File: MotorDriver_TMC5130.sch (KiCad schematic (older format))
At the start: 17 parts, among them U8 TMC5130

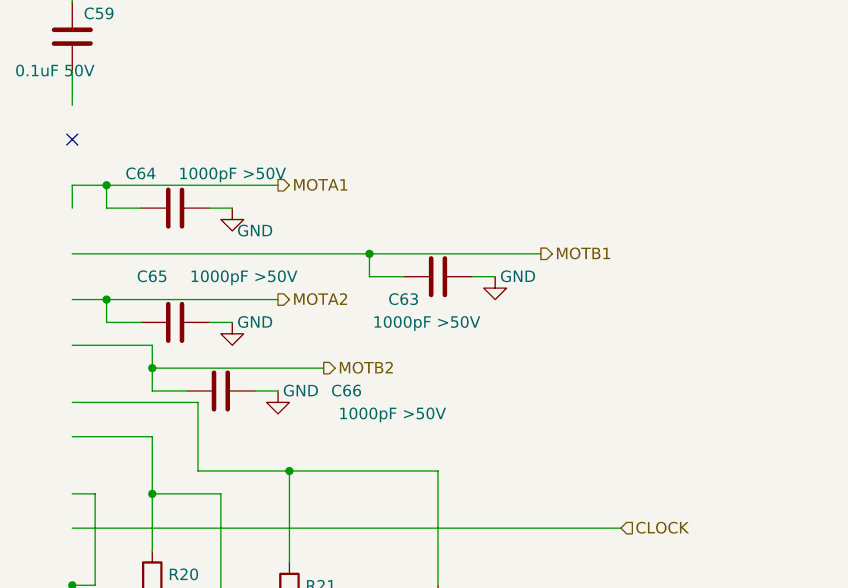
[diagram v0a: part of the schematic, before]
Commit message: Changed 1000pF capacitor value in teh motor drivers.
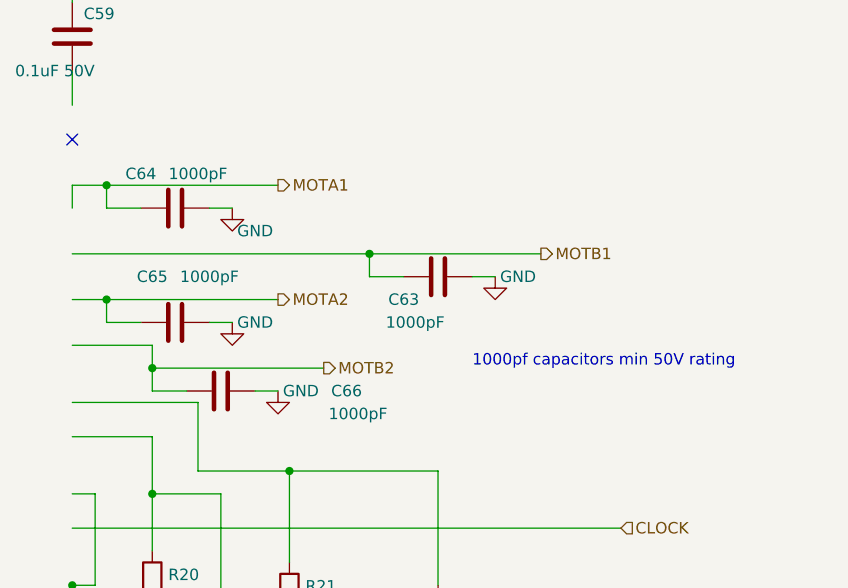
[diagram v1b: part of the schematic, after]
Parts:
- C10, C11, C12, C13: value 1000pF >50V -> 1000pF
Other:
- note added: "1000pf capacitors min 50V rating"
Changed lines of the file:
@@
 $Descr A4 11693 8268
 encoding utf-8
-Sheet 17 35
+Sheet 26 35
 Title ""
 Date ""
@@
 AR Path="/5AC337B6/5AD9F95A/5AD4B0F5/5AC33CA1" Ref="C63"  Part="1"
 F 0 "C63" V 7650 3450 50  0000 C CNN
-F 1 "1000pF >50V" V 7750 3550 50  0000 C CNN
+F 1 "1000pF" V 7750 3500 50  0000 C CNN
 F 2 "Capacitor_SMD:C_0603_1608Metric" H 7588 3450 50  0001 C CNN
 F 3 "~" H 7550 3600 50  0001 C CNN
@@
 AR Path="/5AC337B6/5AD9F95A/5AD4B0F5/5AC33D6E" Ref="C64"  Part="1"
 F 0 "C64" V 6250 3150 50  0000 C CNN
-F 1 "1000pF >50V" V 6250 3550 50  0000 C CNN
+F 1 "1000pF" V 6250 3400 50  0000 C CNN
 F 2 "Capacitor_SMD:C_0603_1608Metric" H 6438 3150 50  0001 C CNN
 F 3 "~" H 6400 3300 50  0001 C CNN
@@
 AR Path="/5AC337B6/5AD9F95A/5AD4B0F5/5AC33DC1" Ref="C65"  Part="1"
 F 0 "C65" V 6200 3700 50  0000 C CNN
-F 1 "1000pF >50V" V 6200 4100 50  0000 C CNN
+F 1 "1000pF" V 6200 3950 50  0000 C CNN
 F 2 "Capacitor_SMD:C_0603_1608Metric" H 6438 3650 50  0001 C CNN
 F 3 "~" H 6400 3800 50  0001 C CNN
@@
 AR Path="/5AC337B6/5AD9F95A/5AD4B0F5/5AC33E6E" Ref="C66"  Part="1"
 F 0 "C66" V 6600 4650 50  0000 C CNN
-F 1 "1000pF >50V" V 6700 4850 50  0000 C CNN
+F 1 "1000pF" V 6700 4700 50  0000 C CNN
 F 2 "Capacitor_SMD:C_0603_1608Metric" H 6638 3950 50  0001 C CNN
 F 3 "~" H 6600 4100 50  0001 C CNN
@@
 Wire Wire Line
 	5950 4700 8350 4700
+Text Notes 7700 4000 0    50   ~ 0
+1000pf capacitors min 50V rating
 $EndSCHEMATC

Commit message: Switch away from rounded rect pads. The PCB boar house had issues making the board.
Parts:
- C10, C11, C12, C13, C7, C8, C84, C85: footprint Capacitor_SMD:C_0603_1608Metric -> PrntrBoardV1:C_0603_1608Metric
- C4, C74: footprint Capacitor_SMD:C_1206_3216Metric -> PrntrBoardV1:C_1206_3216Metric
- C6, C86, C87: footprint Capacitor_SMD:C_0402_1005Metric -> PrntrBoardV1:C_0402_1005Metric
- R20, R21: footprint Resistor_SMD:R_1206_3216Metric -> PrntrBoardV1:R_1206_3216Metric
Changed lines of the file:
@@
 AR Path="/5AC337B6/5ACE1C6D/5ACC0B66/5AC33A94" Ref="C46"  Part="1"
 AR Path="/5AC337B6/5AD9F95A/5AD4B0F5/5AC33A94" Ref="C59"  Part="1"
-F 0 "C59" H 6000 2650 50  0000 L CNN
+F 0 "C6" H 6000 2650 50  0000 L CNN
 F 1 "0.1uF 50V" H 5700 2400 50  0000 L CNN
-F 2 "Capacitor_SMD:C_0402_1005Metric" H 5988 2400 50  0001 C CNN
+F 2 "PrntrBoardV1:C_0402_1005Metric" H 5988 2400 50  0001 C CNN
 F 3 "~" H 5950 2550 50  0001 C CNN
 	1    5950 2550
@@
 AR Path="/5AC337B6/5ACE1C6D/5ACC0B66/5AC33B3C" Ref="C44"  Part="1"
 AR Path="/5AC337B6/5AD9F95A/5AD4B0F5/5AC33B3C" Ref="C57"  Part="1"
-F 0 "C57" H 3050 1750 50  0000 L CNN
+F 0 "C4" H 3050 1750 50  0000 L CNN
 F 1 "10uF 50V" H 2850 1650 50  0000 L CNN
-F 2 "Capacitor_SMD:C_1206_3216Metric" H 3338 1550 50  0001 C CNN
+F 2 "PrntrBoardV1:C_1206_3216Metric" H 3338 1550 50  0001 C CNN
 F 3 "~" H 3300 1700 50  0001 C CNN
 	1    3300 1700
@@
 AR Path="/5AC337B6/5ACE1C6D/5ACC0B66/5AC33B85" Ref="C47"  Part="1"
 AR Path="/5AC337B6/5AD9F95A/5AD4B0F5/5AC33B85" Ref="C60"  Part="1"
-F 0 "C60" H 5250 1800 50  0000 C CNN
+F 0 "C7" H 5250 1800 50  0000 C CNN
 F 1 "0.47uF" H 5200 1700 50  0000 C CNN
-F 2 "Capacitor_SMD:C_0603_1608Metric" H 5488 1650 50  0001 C CNN
+F 2 "PrntrBoardV1:C_0603_1608Metric" H 5488 1650 50  0001 C CNN
 F 3 "~" H 5450 1800 50  0001 C CNN
 	1    5450 1800
@@
 AR Path="/5AC337B6/5ACE1C6D/5ACC0B66/5AC33C56" Ref="C48"  Part="1"
 AR Path="/5AC337B6/5AD9F95A/5AD4B0F5/5AC33C56" Ref="C61"  Part="1"
-F 0 "C61" H 4315 2096 50  0000 L CNN
+F 0 "C8" H 4315 2096 50  0000 L CNN
 F 1 "0.1uF" H 4315 2005 50  0000 L CNN
-F 2 "Capacitor_SMD:C_0603_1608Metric" H 4238 1900 50  0001 C CNN
+F 2 "PrntrBoardV1:C_0603_1608Metric" H 4238 1900 50  0001 C CNN
 F 3 "~" H 4200 2050 50  0001 C CNN
 	1    4200 2050
@@
 AR Path="/5AC337B6/5ACE1C6D/5ACC0B66/5AC33CA1" Ref="C50"  Part="1"
 AR Path="/5AC337B6/5AD9F95A/5AD4B0F5/5AC33CA1" Ref="C63"  Part="1"
-F 0 "C63" V 7650 3450 50  0000 C CNN
+F 0 "C10" V 7650 3450 50  0000 C CNN
 F 1 "1000pF" V 7750 3500 50  0000 C CNN
-F 2 "Capacitor_SMD:C_0603_1608Metric" H 7588 3450 50  0001 C CNN
+F 2 "PrntrBoardV1:C_0603_1608Metric" H 7588 3450 50  0001 C CNN
 F 3 "~" H 7550 3600 50  0001 C CNN
 	1    7550 3600
@@
 AR Path="/5AC337B6/5ACE1C6D/5ACC0B66/5AC33D6E" Ref="C51"  Part="1"
 AR Path="/5AC337B6/5AD9F95A/5AD4B0F5/5AC33D6E" Ref="C64"  Part="1"
-F 0 "C64" V 6250 3150 50  0000 C CNN
+F 0 "C11" V 6250 3150 50  0000 C CNN
 F 1 "1000pF" V 6250 3400 50  0000 C CNN
-F 2 "Capacitor_SMD:C_0603_1608Metric" H 6438 3150 50  0001 C CNN
+F 2 "PrntrBoardV1:C_0603_1608Metric" H 6438 3150 50  0001 C CNN
 F 3 "~" H 6400 3300 50  0001 C CNN
 	1    6400 3300
@@
 AR Path="/5AC337B6/5ACE1C6D/5ACC0B66/5AC33DC1" Ref="C52"  Part="1"
 AR Path="/5AC337B6/5AD9F95A/5AD4B0F5/5AC33DC1" Ref="C65"  Part="1"
-F 0 "C65" V 6200 3700 50  0000 C CNN
+F 0 "C12" V 6200 3700 50  0000 C CNN
 F 1 "1000pF" V 6200 3950 50  0000 C CNN
-F 2 "Capacitor_SMD:C_0603_1608Metric" H 6438 3650 50  0001 C CNN
+F 2 "PrntrBoardV1:C_0603_1608Metric" H 6438 3650 50  0001 C CNN
 F 3 "~" H 6400 3800 50  0001 C CNN
 	1    6400 3800
@@
 AR Path="/5AC337B6/5ACE1C6D/5ACC0B66/5AC33E6E" Ref="C53"  Part="1"
 AR Path="/5AC337B6/5AD9F95A/5AD4B0F5/5AC33E6E" Ref="C66"  Part="1"
-F 0 "C66" V 6600 4650 50  0000 C CNN
+F 0 "C13" V 6600 4650 50  0000 C CNN
 F 1 "1000pF" V 6700 4700 50  0000 C CNN
-F 2 "Capacitor_SMD:C_0603_1608Metric" H 6638 3950 50  0001 C CNN
+F 2 "PrntrBoardV1:C_0603_1608Metric" H 6638 3950 50  0001 C CNN
 F 3 "~" H 6600 4100 50  0001 C CNN
 	1    6600 4100
@@
 AR Path="/5AC337B6/5ACE1C6D/5ACC0B66/5AC34593" Ref="#PWR049"  Part="1"
 AR Path="/5AC337B6/5AD9F95A/5AD4B0F5/5AC34593" Ref="#PWR059"  Part="1"
-F 0 "#PWR059" H 5450 1950 50  0001 C CNN
+F 0 "#PWR014" H 5450 1950 50  0001 C CNN
 F 1 "GND" H 5455 2027 50  0000 C CNN
 F 2 "" H 5450 2200 50  0001 C CNN
@@
 AR Path="/5AC337B6/5ACE1C6D/5ACC0B66/5AC345D6" Ref="#PWR048"  Part="1"
 AR Path="/5AC337B6/5AD9F95A/5AD4B0F5/5AC345D6" Ref="#PWR058"  Part="1"
-F 0 "#PWR058" H 3300 1800 50  0001 C CNN
+F 0 "#PWR013" H 3300 1800 50  0001 C CNN
 F 1 "GND" H 3305 1877 50  0000 C CNN
 F 2 "" H 3300 2050 50  0001 C CNN
@@
 AR Path="/5AC337B6/5ACE1C6D/5ACC0B66/5AC34619" Ref="#PWR050"  Part="1"
 AR Path="/5AC337B6/5AD9F95A/5AD4B0F5/5AC34619" Ref="#PWR060"  Part="1"
-F 0 "#PWR060" H 7800 3350 50  0001 C CNN
+F 0 "#PWR015" H 7800 3350 50  0001 C CNN
 F 1 "GND" H 7900 3600 50  0000 C CNN
 F 2 "" H 7800 3600 50  0001 C CNN
@@
 AR Path="/5AC337B6/5ACE1C6D/5ACC0B66/5AC3465C" Ref="#PWR051"  Part="1"
 AR Path="/5AC337B6/5AD9F95A/5AD4B0F5/5AC3465C" Ref="#PWR061"  Part="1"
-F 0 "#PWR061" H 6650 3050 50  0001 C CNN
+F 0 "#PWR016" H 6650 3050 50  0001 C CNN
 F 1 "GND" H 6750 3200 50  0000 C CNN
 F 2 "" H 6650 3300 50  0001 C CNN
@@
 AR Path="/5AC337B6/5ACE1C6D/5ACC0B66/5AC3469F" Ref="#PWR052"  Part="1"
 AR Path="/5AC337B6/5AD9F95A/5AD4B0F5/5AC3469F" Ref="#PWR062"  Part="1"
-F 0 "#PWR062" H 6650 3550 50  0001 C CNN
+F 0 "#PWR017" H 6650 3550 50  0001 C CNN
 F 1 "GND" H 6750 3800 50  0000 C CNN
 F 2 "" H 6650 3800 50  0001 C CNN
@@
 AR Path="/5AC337B6/5ACE1C6D/5ACC0B66/5AC346E2" Ref="#PWR053"  Part="1"
 AR Path="/5AC337B6/5AD9F95A/5AD4B0F5/5AC346E2" Ref="#PWR063"  Part="1"
-F 0 "#PWR063" H 6850 3850 50  0001 C CNN
+F 0 "#PWR018" H 6850 3850 50  0001 C CNN
 F 1 "GND" H 6950 4100 50  0000 C CNN
 F 2 "" H 6850 4100 50  0001 C CNN
@@
 AR Path="/5AC337B6/5ACE1C6D/5ACC0B66/5AC34725" Ref="#PWR047"  Part="1"
 AR Path="/5AC337B6/5AD9F95A/5AD4B0F5/5AC34725" Ref="#PWR057"  Part="1"
-F 0 "#PWR057" H 5350 5550 50  0001 C CNN
+F 0 "#PWR012" H 5350 5550 50  0001 C CNN
 F 1 "GND" H 5355 5627 50  0000 C CNN
 F 2 "" H 5350 5800 50  0001 C CNN
@@
 AR Path="/5AC337B6/5ACE1C6D/5ACC0B66/5AC55FA7" Ref="C45"  Part="1"
 AR Path="/5AC337B6/5AD9F95A/5AD4B0F5/5AC55FA7" Ref="C58"  Part="1"
-F 0 "C58" H 3700 1900 50  0000 L CNN
+F 0 "C5" H 3700 1900 50  0000 L CNN
 F 1 "100uF 35V" H 3700 1800 50  0000 L CNN
 F 2 "Capacitor_SMD:CP_Elec_6.3x7.7" H 3650 1700 50  0001 C CNN
@@
 AR Path="/5AC337B6/5ACE1C6D/5ACC0B66/5ACA36B2" Ref="C76"  Part="1"
 AR Path="/5AC337B6/5AD9F95A/5AD4B0F5/5ACA36B2" Ref="C77"  Part="1"
-F 0 "C77" H 2715 1746 50  0000 L CNN
+F 0 "C73" H 2715 1746 50  0000 L CNN
 F 1 "10uF 50V" H 2650 1550 50  0000 L CNN
-F 2 "Capacitor_SMD:C_1206_3216Metric" H 2638 1550 50  0001 C CNN
+F 2 "PrntrBoardV1:C_1206_3216Metric" H 2638 1550 50  0001 C CNN
 F 3 "~" H 2600 1700 50  0001 C CNN
 	1    2600 1700
@@
 AR Path="/5AC337B6/5ACCA309/5ACC0B66/5ACFA54E" Ref="U6"  Part="1"
 AR Path="/5AC337B6/5ACE1C6D/5ACC0B66/5ACFA54E" Ref="U7"  Part="1"
-F 0 "U8" H 4900 1714 50  0000 C CNN
+F 0 "U4" H 4900 1714 50  0000 C CNN
 F 1 "TMC5130" H 4900 1623 50  0000 C CNN
 F 2 "PrntrBoardV1:tmc5130-nc" H 4900 3700 50  0001 C CNN
@@
 AR Path="/5AC337B6/5ACCA309/5ACC0B66/5AD3397E" Ref="#PWR081"  Part="1"
 AR Path="/5AC337B6/5ACE1C6D/5ACC0B66/5AD3397E" Ref="#PWR083"  Part="1"
-F 0 "#PWR085" H 4200 2000 50  0001 C CNN
+F 0 "#PWR077" H 4200 2000 50  0001 C CNN
 F 1 "GND" H 4205 2077 50  0000 C CNN
 F 2 "" H 4200 2250 50  0001 C CNN
@@
 AR Path="/5AC337B6/5ACCA309/5ACC0B66/5AD37DE9" Ref="C67"  Part="1"
 AR Path="/5AC337B6/5ACE1C6D/5ACC0B66/5AD37DE9" Ref="C81"  Part="1"
-F 0 "C85" H 5000 2350 50  0000 L CNN
+F 0 "C14" H 5000 2350 50  0000 L CNN
 F 1 "0.1uF" H 4900 2250 50  0000 L CNN
-F 2 "Capacitor_SMD:C_0603_1608Metric" H 5188 2000 50  0001 C CNN
+F 2 "PrntrBoardV1:C_0603_1608Metric" H 5188 2000 50  0001 C CNN
 F 3 "~" H 5150 2150 50  0001 C CNN
 	1    5150 2150
@@
 AR Path="/5AC337B6/5ACCA309/5ACC0B66/5AD494C8" Ref="C62"  Part="1"
 AR Path="/5AC337B6/5ACE1C6D/5ACC0B66/5AD494C8" Ref="C80"  Part="1"
-F 0 "C84" V 3750 5200 50  0000 C CNN
+F 0 "C9" V 3750 5200 50  0000 C CNN
 F 1 "0.022uF 50V" V 3750 4750 50  0000 C CNN
-F 2 "Capacitor_SMD:C_0603_1608Metric" H 3638 4900 50  0001 C CNN
+F 2 "PrntrBoardV1:C_0603_1608Metric" H 3638 4900 50  0001 C CNN
 F 3 "~" H 3600 5050 50  0001 C CNN
 	1    3600 5050
@@
 AR Path="/5AC337B6/5ACCA309/5ACC0B66/5AD5670C" Ref="#PWR080"  Part="1"
 AR Path="/5AC337B6/5ACE1C6D/5ACC0B66/5AD5670C" Ref="#PWR082"  Part="1"
-F 0 "#PWR084" H 3600 3900 50  0001 C CNN
+F 0 "#PWR076" H 3600 3900 50  0001 C CNN
 F 1 "GND" H 3605 3977 50  0000 C CNN
 F 2 "" H 3600 4150 50  0001 C CNN
@@
 AR Path="/5AC337B6/5ACCA309/5ACC0B66/5AD66FAA" Ref="R12"  Part="1"
 AR Path="/5AC337B6/5ACE1C6D/5ACC0B66/5AD66FAA" Ref="R14"  Part="1"
-F 0 "R20" H 6370 4996 50  0000 L CNN
+F 0 "R2" H 6370 4996 50  0000 L CNN
 F 1 "0R15 0.5W" H 6100 4800 50  0000 L CNN
-F 2 "Resistor_SMD:R_1206_3216Metric" V 6230 4950 50  0001 C CNN
+F 2 "PrntrBoardV1:R_1206_3216Metric" V 6230 4950 50  0001 C CNN
 F 3 "~" H 6300 4950 50  0001 C CNN
 	1    6300 4950
@@
 AR Path="/5AC337B6/5ACCA309/5ACC0B66/5AD67008" Ref="R13"  Part="1"
 AR Path="/5AC337B6/5ACE1C6D/5ACC0B66/5AD67008" Ref="R15"  Part="1"
-F 0 "R21" H 6970 5046 50  0000 L CNN
+F 0 "R3" H 6970 5046 50  0000 L CNN
 F 1 "0R15 0.5W" H 6970 4955 50  0000 L CNN
-F 2 "Resistor_SMD:R_1206_3216Metric" V 6830 5000 50  0001 C CNN
+F 2 "PrntrBoardV1:R_1206_3216Metric" V 6830 5000 50  0001 C CNN
 F 3 "~" H 6900 5000 50  0001 C CNN
 	1    6900 5000
@@
 AR Path="/5AC337B6/5ACCA309/5ACC0B66/5AD6F856" Ref="C79"  Part="1"
 AR Path="/5AC337B6/5ACE1C6D/5ACC0B66/5AD6F856" Ref="C83"  Part="1"
-F 0 "C87" H 7665 5146 50  0000 L CNN
+F 0 "C28" H 7665 5146 50  0000 L CNN
 F 1 "0.1uF 50V" H 7665 5055 50  0000 L CNN
-F 2 "Capacitor_SMD:C_0402_1005Metric" H 7588 4950 50  0001 C CNN
+F 2 "PrntrBoardV1:C_0402_1005Metric" H 7588 4950 50  0001 C CNN
 F 3 "~" H 7550 5100 50  0001 C CNN
 	1    7550 5100
@@
 AR Path="/5AC337B6/5ACCA309/5ACC0B66/5AD6F966" Ref="C78"  Part="1"
 AR Path="/5AC337B6/5ACE1C6D/5ACC0B66/5AD6F966" Ref="C82"  Part="1"
-F 0 "C86" H 6715 5246 50  0000 L CNN
+F 0 "C23" H 6715 5246 50  0000 L CNN
 F 1 "0.1uF 50V" H 6350 5050 50  0000 L CNN
-F 2 "Capacitor_SMD:C_0402_1005Metric" H 6638 5050 50  0001 C CNN
+F 2 "PrntrBoardV1:C_0402_1005Metric" H 6638 5050 50  0001 C CNN
 F 3 "~" H 6600 5200 50  0001 C CNN
 	1    6600 5200

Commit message: Update schematics to match rev3 of tmc2130 branch.
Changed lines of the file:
@@
 EESchema Schematic File Version 4
 LIBS:PrntrBoardV1-cache
-EELAYER 26 0
+EELAYER 29 0
 EELAYER END
 $Descr A4 11693 8268
@@
 AR Path="/5AC337B6/5ACE1C6D/5ACC0B66/5AC33A94" Ref="C46"  Part="1"
 AR Path="/5AC337B6/5AD9F95A/5AD4B0F5/5AC33A94" Ref="C59"  Part="1"
-F 0 "C6" H 6000 2650 50  0000 L CNN
+F 0 "C59" H 6000 2650 50  0000 L CNN
 F 1 "0.1uF 50V" H 5700 2400 50  0000 L CNN
 F 2 "PrntrBoardV1:C_0402_1005Metric" H 5988 2400 50  0001 C CNN
@@
 AR Path="/5AC337B6/5ACE1C6D/5ACC0B66/5AC33B3C" Ref="C44"  Part="1"
 AR Path="/5AC337B6/5AD9F95A/5AD4B0F5/5AC33B3C" Ref="C57"  Part="1"
-F 0 "C4" H 3050 1750 50  0000 L CNN
+F 0 "C57" H 3050 1750 50  0000 L CNN
 F 1 "10uF 50V" H 2850 1650 50  0000 L CNN
 F 2 "PrntrBoardV1:C_1206_3216Metric" H 3338 1550 50  0001 C CNN
@@
 AR Path="/5AC337B6/5ACE1C6D/5ACC0B66/5AC33B85" Ref="C47"  Part="1"
 AR Path="/5AC337B6/5AD9F95A/5AD4B0F5/5AC33B85" Ref="C60"  Part="1"
-F 0 "C7" H 5250 1800 50  0000 C CNN
+F 0 "C60" H 5250 1800 50  0000 C CNN
 F 1 "0.47uF" H 5200 1700 50  0000 C CNN
 F 2 "PrntrBoardV1:C_0603_1608Metric" H 5488 1650 50  0001 C CNN
@@
 AR Path="/5AC337B6/5ACE1C6D/5ACC0B66/5AC33C56" Ref="C48"  Part="1"
 AR Path="/5AC337B6/5AD9F95A/5AD4B0F5/5AC33C56" Ref="C61"  Part="1"
-F 0 "C8" H 4315 2096 50  0000 L CNN
+F 0 "C61" H 4315 2096 50  0000 L CNN
 F 1 "0.1uF" H 4315 2005 50  0000 L CNN
 F 2 "PrntrBoardV1:C_0603_1608Metric" H 4238 1900 50  0001 C CNN
@@
 AR Path="/5AC337B6/5ACE1C6D/5ACC0B66/5AC33CA1" Ref="C50"  Part="1"
 AR Path="/5AC337B6/5AD9F95A/5AD4B0F5/5AC33CA1" Ref="C63"  Part="1"
-F 0 "C10" V 7650 3450 50  0000 C CNN
+F 0 "C63" V 7650 3450 50  0000 C CNN
 F 1 "1000pF" V 7750 3500 50  0000 C CNN
 F 2 "PrntrBoardV1:C_0603_1608Metric" H 7588 3450 50  0001 C CNN
@@
 AR Path="/5AC337B6/5ACE1C6D/5ACC0B66/5AC33D6E" Ref="C51"  Part="1"
 AR Path="/5AC337B6/5AD9F95A/5AD4B0F5/5AC33D6E" Ref="C64"  Part="1"
-F 0 "C11" V 6250 3150 50  0000 C CNN
+F 0 "C64" V 6250 3150 50  0000 C CNN
 F 1 "1000pF" V 6250 3400 50  0000 C CNN
 F 2 "PrntrBoardV1:C_0603_1608Metric" H 6438 3150 50  0001 C CNN
@@
 AR Path="/5AC337B6/5ACE1C6D/5ACC0B66/5AC33DC1" Ref="C52"  Part="1"
 AR Path="/5AC337B6/5AD9F95A/5AD4B0F5/5AC33DC1" Ref="C65"  Part="1"
-F 0 "C12" V 6200 3700 50  0000 C CNN
+F 0 "C65" V 6200 3700 50  0000 C CNN
 F 1 "1000pF" V 6200 3950 50  0000 C CNN
 F 2 "PrntrBoardV1:C_0603_1608Metric" H 6438 3650 50  0001 C CNN
@@
 AR Path="/5AC337B6/5ACE1C6D/5ACC0B66/5AC33E6E" Ref="C53"  Part="1"
 AR Path="/5AC337B6/5AD9F95A/5AD4B0F5/5AC33E6E" Ref="C66"  Part="1"
-F 0 "C13" V 6600 4650 50  0000 C CNN
+F 0 "C66" V 6600 4650 50  0000 C CNN
 F 1 "1000pF" V 6700 4700 50  0000 C CNN
 F 2 "PrntrBoardV1:C_0603_1608Metric" H 6638 3950 50  0001 C CNN
@@
 AR Path="/5AC337B6/5ACE1C6D/5ACC0B66/5AC34593" Ref="#PWR049"  Part="1"
 AR Path="/5AC337B6/5AD9F95A/5AD4B0F5/5AC34593" Ref="#PWR059"  Part="1"
-F 0 "#PWR014" H 5450 1950 50  0001 C CNN
+F 0 "#PWR059" H 5450 1950 50  0001 C CNN
 F 1 "GND" H 5455 2027 50  0000 C CNN
 F 2 "" H 5450 2200 50  0001 C CNN
@@
 AR Path="/5AC337B6/5ACE1C6D/5ACC0B66/5AC345D6" Ref="#PWR048"  Part="1"
 AR Path="/5AC337B6/5AD9F95A/5AD4B0F5/5AC345D6" Ref="#PWR058"  Part="1"
-F 0 "#PWR013" H 3300 1800 50  0001 C CNN
+F 0 "#PWR058" H 3300 1800 50  0001 C CNN
 F 1 "GND" H 3305 1877 50  0000 C CNN
 F 2 "" H 3300 2050 50  0001 C CNN
@@
 AR Path="/5AC337B6/5ACE1C6D/5ACC0B66/5AC34619" Ref="#PWR050"  Part="1"
 AR Path="/5AC337B6/5AD9F95A/5AD4B0F5/5AC34619" Ref="#PWR060"  Part="1"
-F 0 "#PWR015" H 7800 3350 50  0001 C CNN
+F 0 "#PWR060" H 7800 3350 50  0001 C CNN
 F 1 "GND" H 7900 3600 50  0000 C CNN
 F 2 "" H 7800 3600 50  0001 C CNN
@@
 AR Path="/5AC337B6/5ACE1C6D/5ACC0B66/5AC3465C" Ref="#PWR051"  Part="1"
 AR Path="/5AC337B6/5AD9F95A/5AD4B0F5/5AC3465C" Ref="#PWR061"  Part="1"
-F 0 "#PWR016" H 6650 3050 50  0001 C CNN
+F 0 "#PWR061" H 6650 3050 50  0001 C CNN
 F 1 "GND" H 6750 3200 50  0000 C CNN
 F 2 "" H 6650 3300 50  0001 C CNN
@@
 AR Path="/5AC337B6/5ACE1C6D/5ACC0B66/5AC3469F" Ref="#PWR052"  Part="1"
 AR Path="/5AC337B6/5AD9F95A/5AD4B0F5/5AC3469F" Ref="#PWR062"  Part="1"
-F 0 "#PWR017" H 6650 3550 50  0001 C CNN
+F 0 "#PWR062" H 6650 3550 50  0001 C CNN
 F 1 "GND" H 6750 3800 50  0000 C CNN
 F 2 "" H 6650 3800 50  0001 C CNN
@@
 AR Path="/5AC337B6/5ACE1C6D/5ACC0B66/5AC346E2" Ref="#PWR053"  Part="1"
 AR Path="/5AC337B6/5AD9F95A/5AD4B0F5/5AC346E2" Ref="#PWR063"  Part="1"
-F 0 "#PWR018" H 6850 3850 50  0001 C CNN
+F 0 "#PWR063" H 6850 3850 50  0001 C CNN
 F 1 "GND" H 6950 4100 50  0000 C CNN
 F 2 "" H 6850 4100 50  0001 C CNN
@@
 AR Path="/5AC337B6/5ACE1C6D/5ACC0B66/5AC34725" Ref="#PWR047"  Part="1"
 AR Path="/5AC337B6/5AD9F95A/5AD4B0F5/5AC34725" Ref="#PWR057"  Part="1"
-F 0 "#PWR012" H 5350 5550 50  0001 C CNN
+F 0 "#PWR057" H 5350 5550 50  0001 C CNN
 F 1 "GND" H 5355 5627 50  0000 C CNN
 F 2 "" H 5350 5800 50  0001 C CNN
@@
 AR Path="/5AC337B6/5ACE1C6D/5ACC0B66/5AC55FA7" Ref="C45"  Part="1"
 AR Path="/5AC337B6/5AD9F95A/5AD4B0F5/5AC55FA7" Ref="C58"  Part="1"
-F 0 "C5" H 3700 1900 50  0000 L CNN
+F 0 "C58" H 3700 1900 50  0000 L CNN
 F 1 "100uF 35V" H 3700 1800 50  0000 L CNN
 F 2 "Capacitor_SMD:CP_Elec_6.3x7.7" H 3650 1700 50  0001 C CNN
@@
 AR Path="/5AC337B6/5ACE1C6D/5ACC0B66/5ACA36B2" Ref="C76"  Part="1"
 AR Path="/5AC337B6/5AD9F95A/5AD4B0F5/5ACA36B2" Ref="C77"  Part="1"
-F 0 "C73" H 2715 1746 50  0000 L CNN
+F 0 "C77" H 2715 1746 50  0000 L CNN
 F 1 "10uF 50V" H 2650 1550 50  0000 L CNN
 F 2 "PrntrBoardV1:C_1206_3216Metric" H 2638 1550 50  0001 C CNN
@@
 AR Path="/5AC337B6/5ACCA309/5ACC0B66/5ACFA54E" Ref="U6"  Part="1"
 AR Path="/5AC337B6/5ACE1C6D/5ACC0B66/5ACFA54E" Ref="U7"  Part="1"
-F 0 "U4" H 4900 1714 50  0000 C CNN
+F 0 "U8" H 4900 1714 50  0000 C CNN
 F 1 "TMC5130" H 4900 1623 50  0000 C CNN
 F 2 "PrntrBoardV1:tmc5130-nc" H 4900 3700 50  0001 C CNN
@@
 AR Path="/5AC337B6/5ACCA309/5ACC0B66/5AD3397E" Ref="#PWR081"  Part="1"
 AR Path="/5AC337B6/5ACE1C6D/5ACC0B66/5AD3397E" Ref="#PWR083"  Part="1"
-F 0 "#PWR077" H 4200 2000 50  0001 C CNN
+F 0 "#PWR085" H 4200 2000 50  0001 C CNN
 F 1 "GND" H 4205 2077 50  0000 C CNN
 F 2 "" H 4200 2250 50  0001 C CNN
@@
 AR Path="/5AC337B6/5ACCA309/5ACC0B66/5AD37DE9" Ref="C67"  Part="1"
 AR Path="/5AC337B6/5ACE1C6D/5ACC0B66/5AD37DE9" Ref="C81"  Part="1"
-F 0 "C14" H 5000 2350 50  0000 L CNN
+F 0 "C85" H 5000 2350 50  0000 L CNN
 F 1 "0.1uF" H 4900 2250 50  0000 L CNN
 F 2 "PrntrBoardV1:C_0603_1608Metric" H 5188 2000 50  0001 C CNN
@@
 AR Path="/5AC337B6/5ACCA309/5ACC0B66/5AD494C8" Ref="C62"  Part="1"
 AR Path="/5AC337B6/5ACE1C6D/5ACC0B66/5AD494C8" Ref="C80"  Part="1"
-F 0 "C9" V 3750 5200 50  0000 C CNN
+F 0 "C84" V 3750 5200 50  0000 C CNN
 F 1 "0.022uF 50V" V 3750 4750 50  0000 C CNN
 F 2 "PrntrBoardV1:C_0603_1608Metric" H 3638 4900 50  0001 C CNN
@@
 AR Path="/5AC337B6/5ACCA309/5ACC0B66/5AD5670C" Ref="#PWR080"  Part="1"
 AR Path="/5AC337B6/5ACE1C6D/5ACC0B66/5AD5670C" Ref="#PWR082"  Part="1"
-F 0 "#PWR076" H 3600 3900 50  0001 C CNN
+F 0 "#PWR084" H 3600 3900 50  0001 C CNN
 F 1 "GND" H 3605 3977 50  0000 C CNN
 F 2 "" H 3600 4150 50  0001 C CNN
@@
 AR Path="/5AC337B6/5ACCA309/5ACC0B66/5AD66FAA" Ref="R12"  Part="1"
 AR Path="/5AC337B6/5ACE1C6D/5ACC0B66/5AD66FAA" Ref="R14"  Part="1"
-F 0 "R2" H 6370 4996 50  0000 L CNN
+F 0 "R20" H 6370 4996 50  0000 L CNN
 F 1 "0R15 0.5W" H 6100 4800 50  0000 L CNN
 F 2 "PrntrBoardV1:R_1206_3216Metric" V 6230 4950 50  0001 C CNN
@@
 AR Path="/5AC337B6/5ACCA309/5ACC0B66/5AD67008" Ref="R13"  Part="1"
 AR Path="/5AC337B6/5ACE1C6D/5ACC0B66/5AD67008" Ref="R15"  Part="1"
-F 0 "R3" H 6970 5046 50  0000 L CNN
+F 0 "R21" H 6970 5046 50  0000 L CNN
 F 1 "0R15 0.5W" H 6970 4955 50  0000 L CNN
 F 2 "PrntrBoardV1:R_1206_3216Metric" V 6830 5000 50  0001 C CNN
@@
 AR Path="/5AC337B6/5ACCA309/5ACC0B66/5AD6F856" Ref="C79"  Part="1"
 AR Path="/5AC337B6/5ACE1C6D/5ACC0B66/5AD6F856" Ref="C83"  Part="1"
-F 0 "C28" H 7665 5146 50  0000 L CNN
+F 0 "C87" H 7665 5146 50  0000 L CNN
 F 1 "0.1uF 50V" H 7665 5055 50  0000 L CNN
 F 2 "PrntrBoardV1:C_0402_1005Metric" H 7588 4950 50  0001 C CNN
@@
 AR Path="/5AC337B6/5ACCA309/5ACC0B66/5AD6F966" Ref="C78"  Part="1"
 AR Path="/5AC337B6/5ACE1C6D/5ACC0B66/5AD6F966" Ref="C82"  Part="1"
-F 0 "C23" H 6715 5246 50  0000 L CNN
+F 0 "C86" H 6715 5246 50  0000 L CNN
 F 1 "0.1uF 50V" H 6350 5050 50  0000 L CNN
 F 2 "PrntrBoardV1:C_0402_1005Metric" H 6638 5050 50  0001 C CNN
